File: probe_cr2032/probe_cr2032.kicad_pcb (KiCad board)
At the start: 2 copper layers, 28.2 x 28.2 mm, 24 parts, among them J0 R0, U1 MCP73831-2-OT, U2 LTC3525-5, U3 MCP102-240D

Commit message: - add fix for PCB v1.1 (fix resistor place 1608)
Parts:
-  : value iFly -> Probe Power v1.1
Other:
- board text removed: "© 2025 AeroSoft"
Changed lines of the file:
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@@
     )
     (pad_to_mask_clearance 0)
-    (grid_origin 83.569 103.1044)
+    (grid_origin 118.819 102.1044)
     (pcbplotparams
       (layerselection 0x00010fc_ffffffff)
@@
       (effects (font (size 1.524 1.524) (thickness 0.3)) (justify mirror))
     )
-    (fp_text value "iFly" (at 0.08 -1.105) (layer "B.SilkS") hide
-      (effects (font (size 1.524 1.524) (thickness 0.3)) (justify mirror))
+    (fp_text value "Probe Power v1.1" (at 0.875 -4.325) (layer "B.SilkS")
+      (effects (font (size 1 1) (thickness 0.15)) (justify mirror))
     )
     (fp_poly (pts
@@
   (gr_circle (center 100.002091 88.000172) (end 101.702091 88.000172) (layer "Edge.Cuts") (width 0.1) (fill none))
   (gr_circle (center 89.619 106) (end 91.319 106) (layer "Edge.Cuts") (width 0.1) (fill none))
-  (gr_text "© 2025 \nAeroSoft" (at 100.094 111.7044) (layer "B.SilkS")
-    (effects (font (size 1 1) (thickness 0.15)) (justify mirror))
-  )
   (gr_text "Charger" (at 91.469 95.4794 60) (layer "B.SilkS")
     (effects (font (size 1 1) (thickness 0.15)) (justify mirror))

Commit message: - v .1.1 in prode
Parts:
- removed 5V1, GND1: , TestPoint:TestPoint_Pad_D1.5mm
-  : value Probe Power v1.1 -> Probe Power v1.2
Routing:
- net Net-(CHR1-Pad1): track 7.28 -> 12.7 mm, vias 0 -> 2
- net GND: track 76.2 -> 71.6 mm
- net +5V: track 73.9 -> 69.5 mm
- net Net-(R2-Pad2): track 46.8 -> 47.5 mm
- net Net-(C2-Pad1): track 84.8 -> 84.2 mm
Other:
- board size 28.2 x 28.2 mm -> 28.8 x 28.8 mm

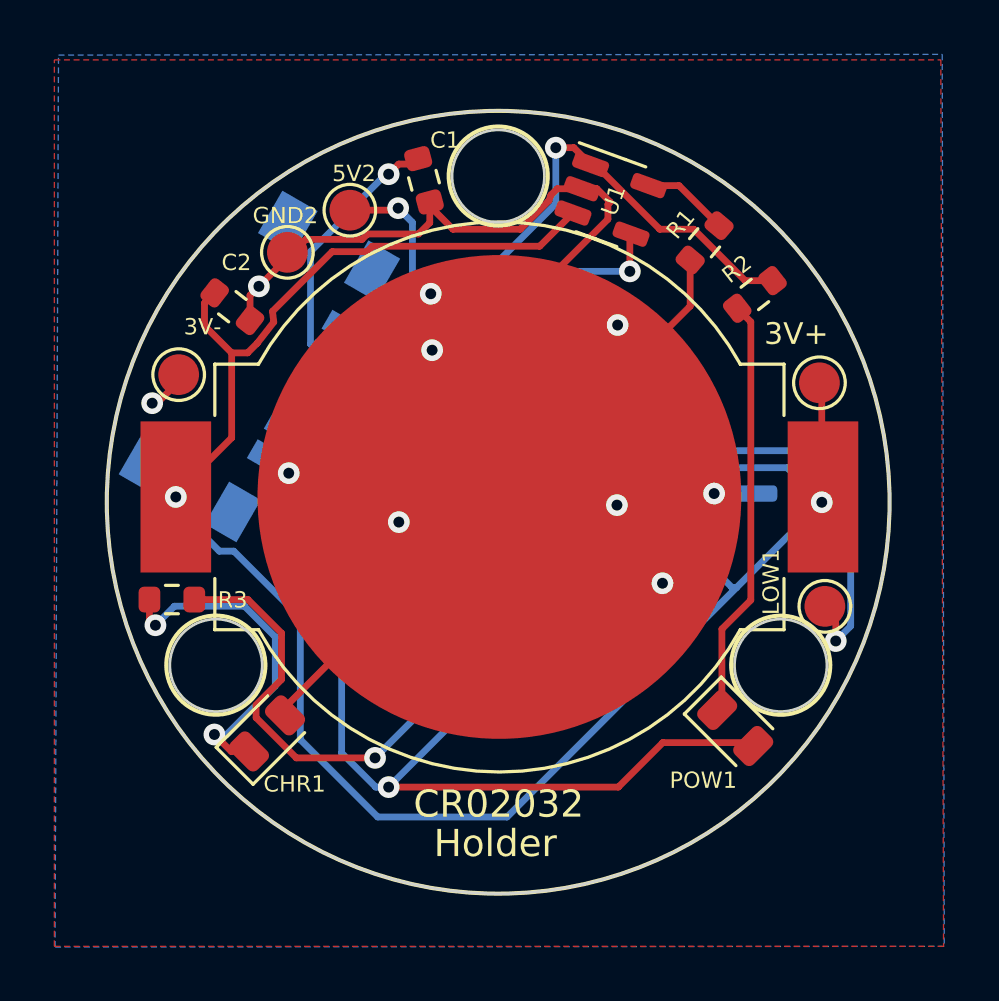
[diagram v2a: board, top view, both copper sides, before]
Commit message: - add lasr fix
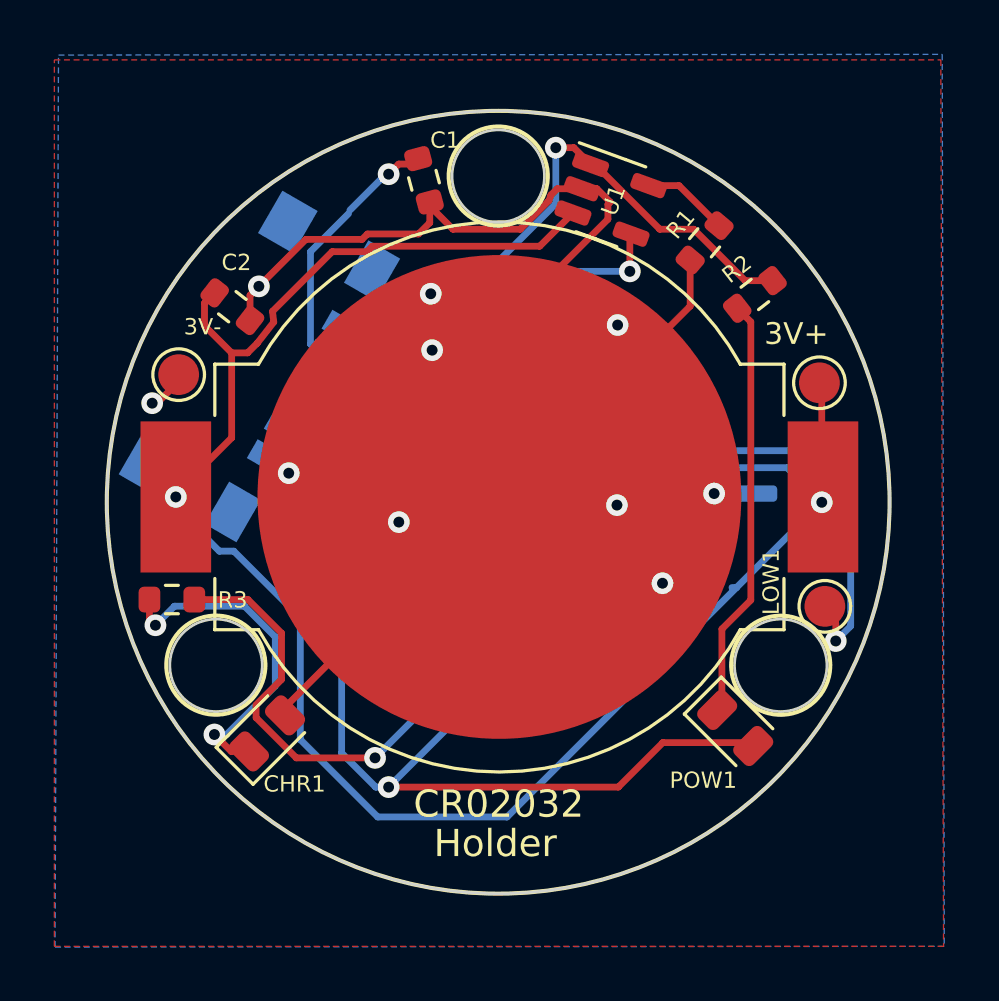
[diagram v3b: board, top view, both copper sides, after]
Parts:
- removed 5V2, GND2: , TestPoint:TestPoint_Pad_D1.5mm
- removed C3: C1uF, Resistor_SMD:R_0603_1608Metric
- removed C4: C22uF, Resistor_SMD:R_0603_1608Metric
- removed J0: R0, Resistor_SMD:R_0201_0603Metric
- removed L1: 10UH, Inductor_SMD:L_Vishay_IFSC-1515AH_4x4x1.8mm
- removed U2: LTC3525-5, Package_TO_SOT_SMD:SOT-363_SC-70-6
-  : value Probe Power v1.2 -> Probe Power v1.3
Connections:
- net +5V renamed Net-(C1-Pad1)
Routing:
- net Net-(5V2-Pad1): track 24.1 -> 0.00 mm, vias 1 -> 0
- net Net-(C3-Pad1): track 22.7 -> 0.00 mm
- net Net-(C2-Pad1): track 84.2 -> 70.0 mm
- net Net-(L1-Pad2): track 12.4 -> 0.00 mm
- net GND: track 71.6 -> 63.2 mm

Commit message: - add new power version
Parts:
- removed U3: MCP102-240D, Package_TO_SOT_SMD:SOT-23
- added J?: Conn_01x03, Connector_Molex:Molex_CLIK-Mate_502386-0370_1x03-1MP_P1.25mm_Horizontal, B.Cu at (100.0, 100.0)
- added U?: APX809-23SAG-7, Package_TO_SOT_SMD:SOT-23, B.Cu at (108.8, 99.6)
- moved   0.95 mm to (100.2, 106.6)
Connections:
- LOW1 pad 1: Net-(LOW1-Pad1) -> unconnected-(LOW1-Pad1)
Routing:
- net unconnected-(LOW1-Pad1): track 0.00 -> 24.4 mm, vias 0 -> 1
- net Net-(LOW1-Pad1): track 17.0 -> 0.00 mm, vias 1 -> 0
- net GND: track 63.2 -> 72.6 mm
- net Net-(C2-Pad1): track 70.0 -> 76.6 mm
- net Net-(R2-Pad2): track 47.5 -> 46.1 mm
- net Net-(C1-Pad1): track 69.5 -> 68.3 mm
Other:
- outline, holes or cut-outs redrawn
